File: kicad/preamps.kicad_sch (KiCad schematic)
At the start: 18 parts, among them U301 LM358, U302 LM358

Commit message: split ch4 and ch5 connectors, update footprints
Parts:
- CD301, CD302: footprint Capacitor_SMD:C_0402_1005Metric -> Custom:C_0402_1005Metric_Fix
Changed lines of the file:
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@@
 			)
 		)
-		(property "Footprint" "Capacitor_SMD:C_0402_1005Metric"
+		(property "Footprint" "Custom:C_0402_1005Metric_Fix"
 			(at 227.0252 152.4 0)
 			(effects
@@
 			)
 		)
-		(property "Footprint" "Capacitor_SMD:C_0402_1005Metric"
+		(property "Footprint" "Custom:C_0402_1005Metric_Fix"
 			(at 253.6952 152.4 0)
 			(effects

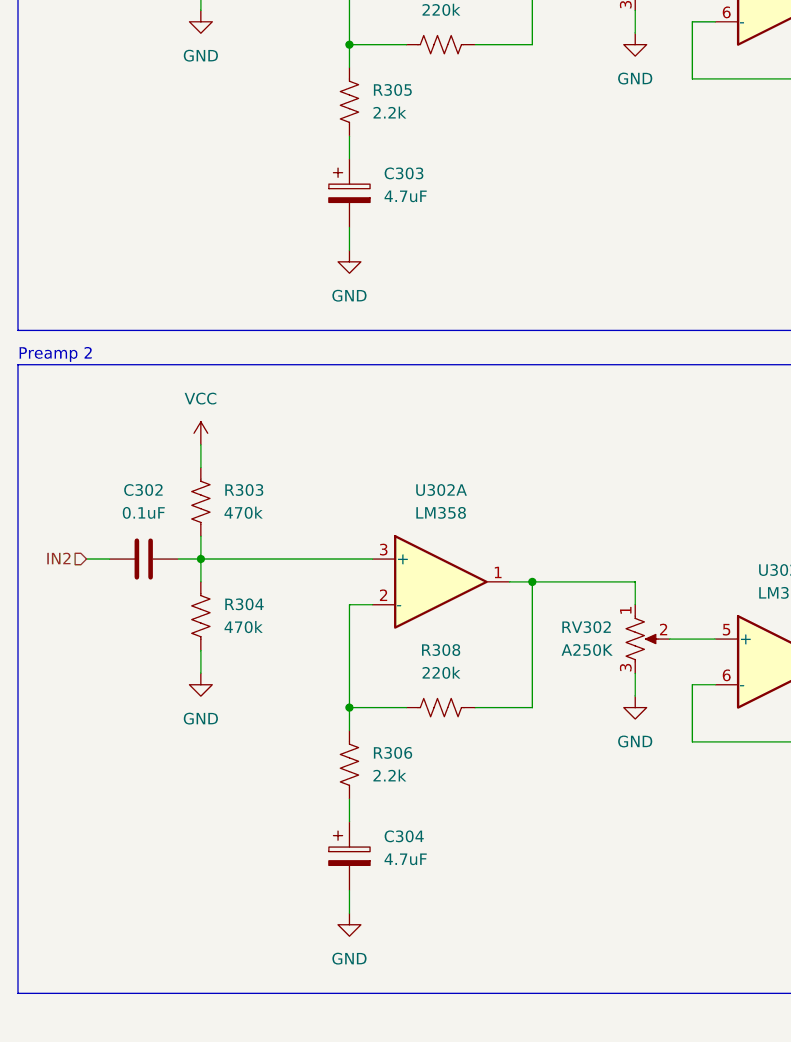
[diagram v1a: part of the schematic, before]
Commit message: replace electrolytic caps with ceramics
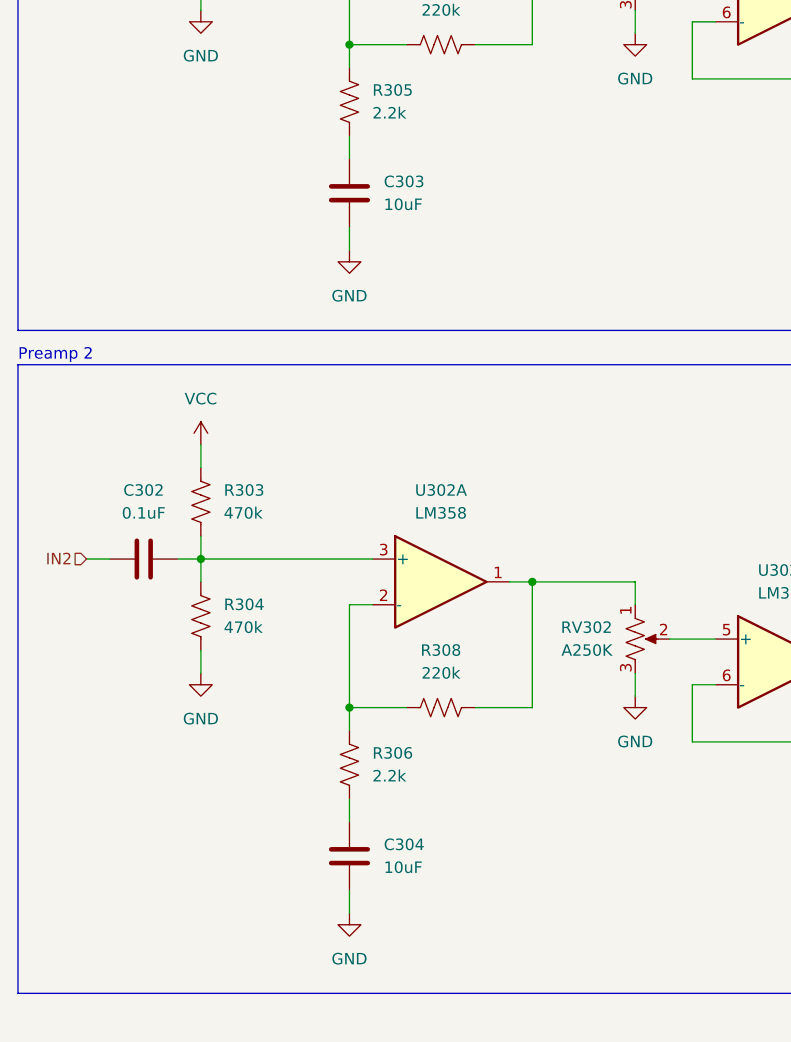
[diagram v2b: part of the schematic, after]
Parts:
- removed C303, C304: 4.7uF, Capacitor_THT:CP_Radial_D5.0mm_P2.00mm, symbol Device:C_Polarized
- added C303, C304: 10uF, Capacitor_SMD:C_1206_3216Metric, symbol Device:C
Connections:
- net GND: now also C303.2, C304.2
- net at R305.2: now also C303.1
- net at R306.2: now also C304.1
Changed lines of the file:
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@@
+	)
+	(symbol
+		(lib_id "Device:C")
+		(at 50.8 144.78 0)
+		(unit 1)
+		(exclude_from_sim no)
+		(in_bom yes)
+		(on_board yes)
+		(dnp no)
+		(fields_autoplaced yes)
+		(property "Reference" "C304"
+			(at 54.61 143.5099 0)
+			(effects
+				(font
+					(size 1.27 1.27)
+				)
+				(justify left)
+			)
+		)
+		(property "Value" "10uF"
+			(at 54.61 146.0499 0)
+			(effects
+				(font
+					(size 1.27 1.27)
+				)
+				(justify left)
+			)
+		)
+		(property "Footprint" "Capacitor_SMD:C_1206_3216Metric"
+			(at 51.7652 148.59 0)
+			(effects
+				(font
+					(size 1.27 1.27)
+				)
+				(hide yes)
+			)
+		)
+		(property "Datasheet" "~"
+			(at 50.8 144.78 0)
+			(effects
+				(font
+					(size 1.27 1.27)
+				)
+				(hide yes)
+			)
+		)
+		(property "Description" "Unpolarized capacitor"
+			(at 50.8 144.78 0)
+			(effects
+				(font
+					(size 1.27 1.27)
+				)
+				(hide yes)
+			)
+		)
+		(property "Supplier" "https://www.digikey.com/en/products/detail/samsung-electro-mechanics/CL31A106KBHNNNE/3888534"
+			(at 50.8 144.78 0)
+			(effects
+				(font
+					(size 1.27 1.27)
+				)
+				(hide yes)
+			)
+		)
+		(pin "2"
+		)
+		(pin "1"
+		)
+		(instances
+			(project "stereo_mixer"
+				(path "/cf7176a5-9cff-4e58-aeea-84be54604336/034aa3da-f36f-4573-9457-c8ef8c02c853"
+					(reference "C304")
+					(unit 1)
+				)
+			)
+		)
 	)
 	(symbol
@@
 	)
 	(symbol
+		(lib_id "Device:C")
+		(at 50.8 71.12 0)
+		(unit 1)
+		(exclude_from_sim no)
+		(in_bom yes)
+		(on_board yes)
+		(dnp no)
+		(fields_autoplaced yes)
+		(property "Reference" "C303"
+			(at 54.61 69.8499 0)
+			(effects
+				(font
+					(size 1.27 1.27)
+				)
+				(justify left)
+			)
+		)
+		(property "Value" "10uF"
+			(at 54.61 72.3899 0)
+			(effects
+				(font
+					(size 1.27 1.27)
+				)
+				(justify left)
+			)
+		)
+		(property "Footprint" "Capacitor_SMD:C_1206_3216Metric"
+			(at 51.7652 74.93 0)
+			(effects
+				(font
+					(size 1.27 1.27)
+				)
+				(hide yes)
+			)
+		)
+		(property "Datasheet" "~"
+			(at 50.8 71.12 0)
+			(effects
+				(font
+					(size 1.27 1.27)
+				)
+				(hide yes)
+			)
+		)
+		(property "Description" "Unpolarized capacitor"
+			(at 50.8 71.12 0)
+			(effects
+				(font
+					(size 1.27 1.27)
+				)
+				(hide yes)
+			)
+		)
+		(property "Supplier" "https://www.digikey.com/en/products/detail/samsung-electro-mechanics/CL31A106KBHNNNE/3888534"
+			(at 50.8 71.12 0)
+			(effects
+				(font
+					(size 1.27 1.27)
+				)
+				(hide yes)
+			)
+		)
+		(pin "2"
+		)
+		(pin "1"
+		)
+		(instances
+			(project "stereo_mixer"
+				(path "/cf7176a5-9cff-4e58-aeea-84be54604336/034aa3da-f36f-4573-9457-c8ef8c02c853"
+					(reference "C303")
+					(unit 1)
+				)
+			)
+		)
+	)
+	(symbol
 		(lib_id "power:GND")
 		(at 34.29 50.8 0)
@@
 	)
 	(symbol
-		(lib_id "Device:C_Polarized")
-		(at 50.8 71.12 0)
-		(unit 1)
-		(exclude_from_sim no)
-		(in_bom yes)
-		(on_board yes)
-		(dnp no)
-		(fields_autoplaced yes)
-		(property "Reference" "C303"
-			(at 54.61 68.9609 0)
-			(effects
-				(font
-					(size 1.27 1.27)
-				)
-				(justify left)
-			)
-		)
-		(property "Value" "4.7uF"
-			(at 54.61 71.5009 0)
-			(effects
-				(font
-					(size 1.27 1.27)
-				)
-				(justify left)
-			)
-		)
-		(property "Footprint" "Capacitor_THT:CP_Radial_D5.0mm_P2.00mm"
-			(at 51.7652 74.93 0)
-			(effects
-				(font
-					(size 1.27 1.27)
-				)
-				(hide yes)
-			)
-		)
-		(property "Datasheet" "~"
-			(at 50.8 71.12 0)
-			(effects
-				(font
-					(size 1.27 1.27)
-				)
-				(hide yes)
-			)
-		)
-		(property "Description" "Polarized capacitor"
-			(at 50.8 71.12 0)
-			(effects
-				(font
-					(size 1.27 1.27)
-				)
-				(hide yes)
-			)
-		)
-		(property "Supplier" "https://www.digikey.com/en/products/detail/w%C3%BCrth-elektronik/860020572001/5727170"
-			(at 50.8 71.12 0)
-			(effects
-				(font
-					(size 1.27 1.27)
-				)
-				(hide yes)
-			)
-		)
-		(pin "2"
-		)
-		(pin "1"
-		)
-		(instances
-			(project ""
-				(path "/cf7176a5-9cff-4e58-aeea-84be54604336/034aa3da-f36f-4573-9457-c8ef8c02c853"
-					(reference "C303")
-					(unit 1)
-				)
-			)
-		)
-	)
-	(symbol
 		(lib_id "power:GND")
 		(at 50.8 77.47 0)
@@
 					(unit 1)
 				)
-			)
-		)
-	)
-	(symbol
-		(lib_id "Device:C_Polarized")
-		(at 50.8 144.78 0)
-		(unit 1)
-		(exclude_from_sim no)
-		(in_bom yes)
-		(on_board yes)
-		(dnp no)
-		(fields_autoplaced yes)
-		(property "Reference" "C304"
-			(at 54.61 142.6209 0)
-			(effects
-				(font
-					(size 1.27 1.27)
-				)
-				(justify left)
-			)
-		)
-		(property "Value" "4.7uF"
-			(at 54.61 145.1609 0)
-			(effects
-				(font
-					(size 1.27 1.27)
-				)
-				(justify left)
-			)
-		)
-		(property "Footprint" "Capacitor_THT:CP_Radial_D5.0mm_P2.00mm"
-			(at 51.7652 148.59 0)
-			(effects
-				(font
-					(size 1.27 1.27)
-				)
-				(hide yes)
-			)
-		)
-		(property "Datasheet" "~"
-			(at 50.8 144.78 0)
-			(effects
-				(font
-					(size 1.27 1.27)
-				)
-				(hide yes)
-			)
-		)
-		(property "Description" "Polarized capacitor"
-			(at 50.8 144.78 0)
-			(effects
-				(font
-					(size 1.27 1.27)
-				)
-				(hide yes)
-			)
-		)
-		(property "Supplier" "https://www.digikey.com/en/products/detail/w%C3%BCrth-elektronik/860020572001/5727170"
-			(at 50.8 144.78 0)
-			(effects
-				(font
-					(size 1.27 1.27)
-				)
-				(hide yes)
-			)
-		)
-		(pin "2"
-		)
-		(pin "1"
-		)
-		(instances
-			(project "stereo_mixer"
-				(path "/cf7176a5-9cff-4e58-aeea-84be54604336/034aa3da-f36f-4573-9457-c8ef8c02c853"
-					(reference "C304")
-					(unit 1)
-				)

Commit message: update preamp potentiometer footprints
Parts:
- RV301, RV302: footprint Connector_Wire:SolderWire-0.25sqmm_1x03_P4.2mm_D0.65mm_OD1.7mm -> Custom:ChassisMount_Wire-0.25sqmm_1x03_P4.2mm_D0.65mm_OD1.7mm
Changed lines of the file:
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@@
 			)
 		)
-		(property "Footprint" "Connector_Wire:SolderWire-0.25sqmm_1x03_P4.2mm_D0.65mm_OD1.7mm"
+		(property "Footprint" "Custom:ChassisMount_Wire-0.25sqmm_1x03_P4.2mm_D0.65mm_OD1.7mm"
 			(at 82.55 120.65 0)
 			(effects
@@
 			)
 		)
-		(property "Footprint" "Connector_Wire:SolderWire-0.25sqmm_1x03_P4.2mm_D0.65mm_OD1.7mm"
+		(property "Footprint" "Custom:ChassisMount_Wire-0.25sqmm_1x03_P4.2mm_D0.65mm_OD1.7mm"
 			(at 82.55 46.99 0)
 			(effects
